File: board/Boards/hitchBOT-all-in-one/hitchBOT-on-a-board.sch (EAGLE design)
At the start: 25 parts, among them Q1 SPD30P06PTO252, Q2 SPD30P06PTO252

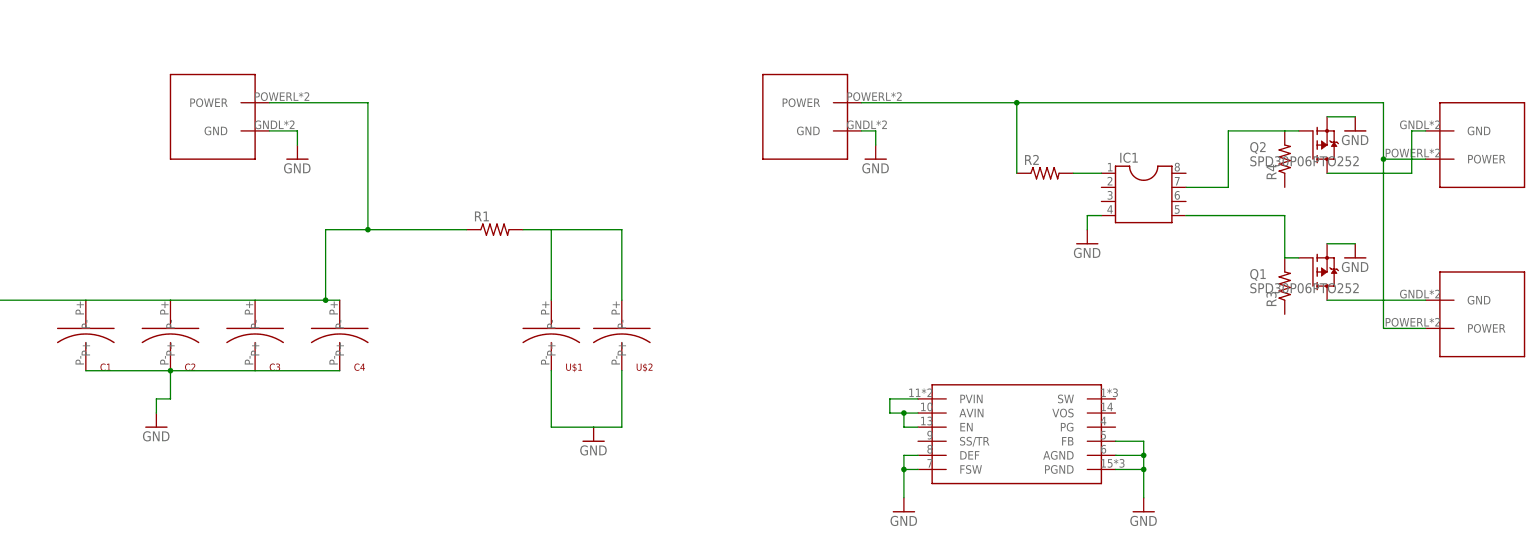
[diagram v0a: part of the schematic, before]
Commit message: finished initial rough copy of the board, need to add LEDs and writing
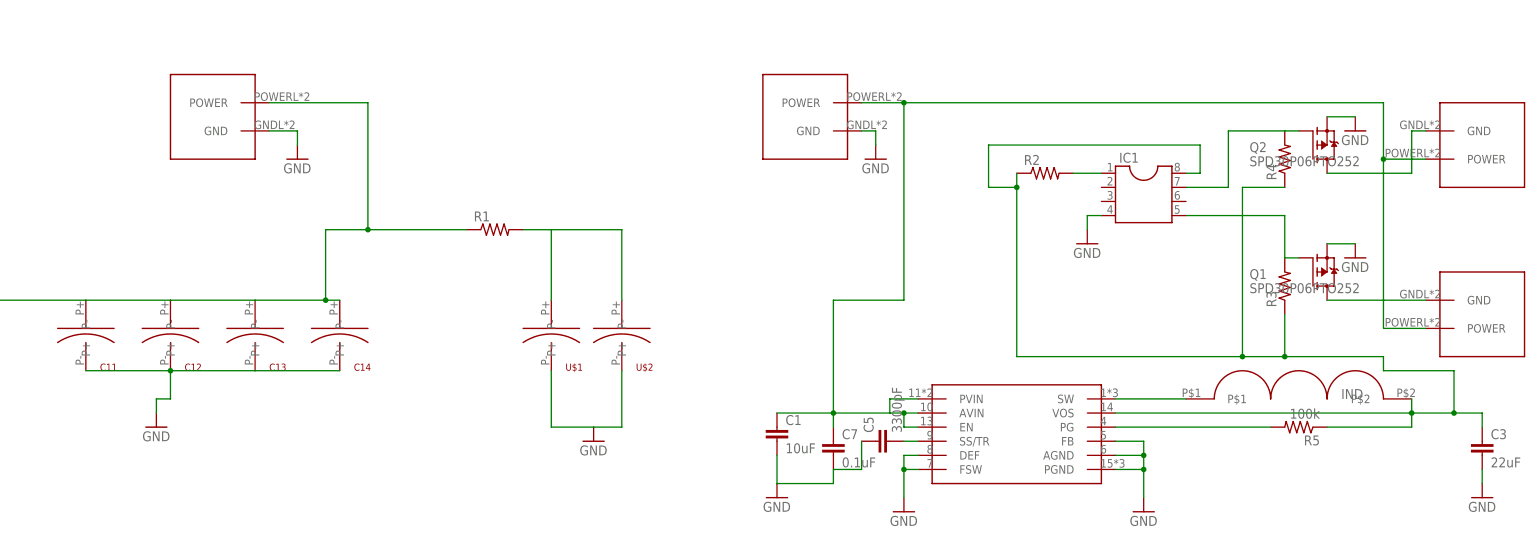
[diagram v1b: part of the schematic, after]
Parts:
- added C11, C13: SMD-CAP-NICHICON-8MM, macgrid:SMD-CAP-NICHICON-8MM
- added C5: 3300pF, rcl:C-EUC0603
- added C7: 0.1uF, rcl:C-EUC0603
- added R5: 100k, resistor:R-US_R1206
- added U$15: DR73-2R2-R, macgrid:DR73-2R2-R
- C1: value SMD-CAP-NICHICON-8MM -> 10uF; device macgrid:SMD-CAP-NICHICON-8MM -> eagle-ltspice:CC1210
- C3: value SMD-CAP-NICHICON-8MM -> 22uF; device macgrid:SMD-CAP-NICHICON-8MM -> rcl:C-EUC0805
- renumbered C2 to C12, C4 to C14
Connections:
- removed net N$12: U$14.AVIN, U$14.EN, U$14.PVIN
- new net N$14: U$14.SW, U$15.P$1
- new net N$15: C3.1, IC1.8, R2.1, R3.1, R4.1, R5.1, U$14.VOS, U$15.P$2
- new net N$16: R5.2, U$14.PG
- new net N$17: C5.2, U$14.SS/TR
- net GND: now also C1.2, C11.P-, C13.P-, C3.2, C5.1, C7.2; no longer C1.P-, C3.P-
- net N$1: now also C11.P+, C13.P+; no longer C1.P+, C3.P+
- net N$8: now also C1.1, C7.1, U$14.AVIN, U$14.EN, U$14.PVIN; no longer R2.1

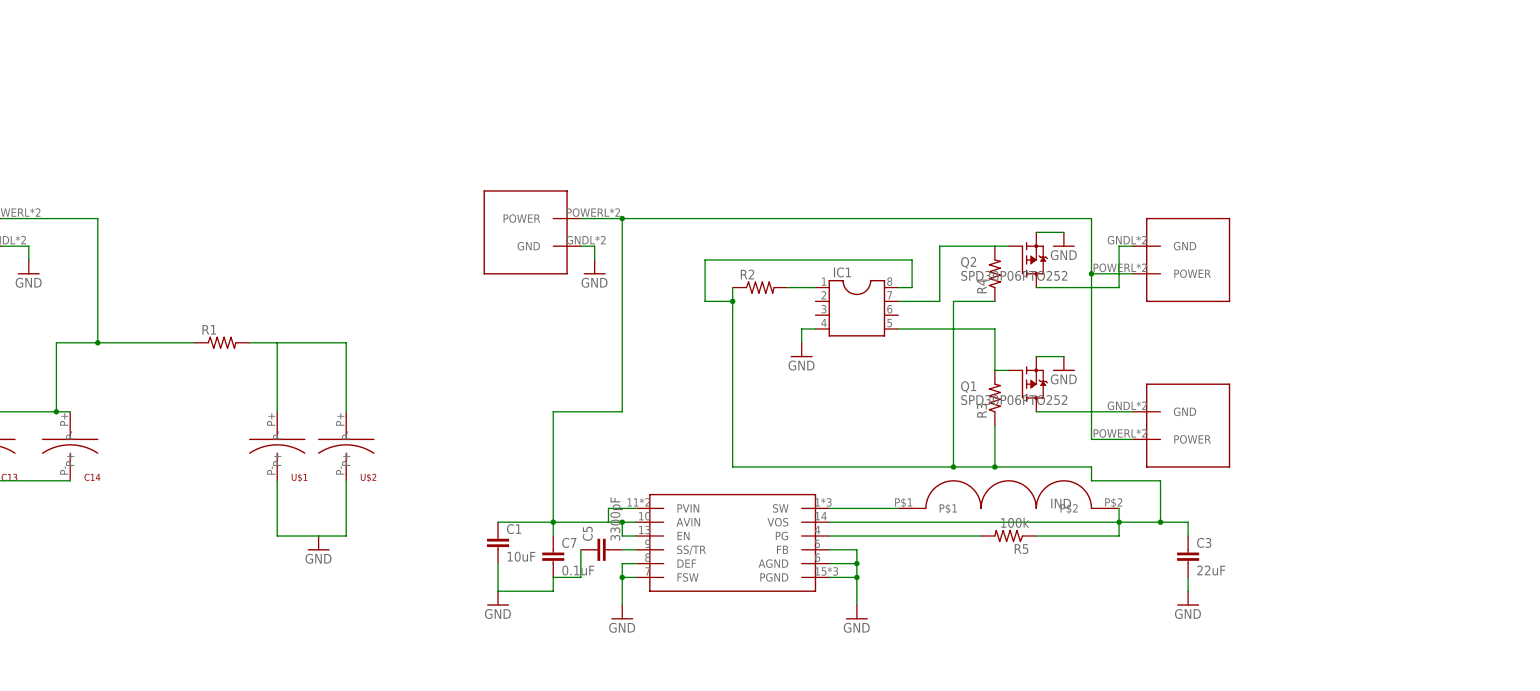
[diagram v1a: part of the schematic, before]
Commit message: added status LED and molex power adapters for all three voltage areas
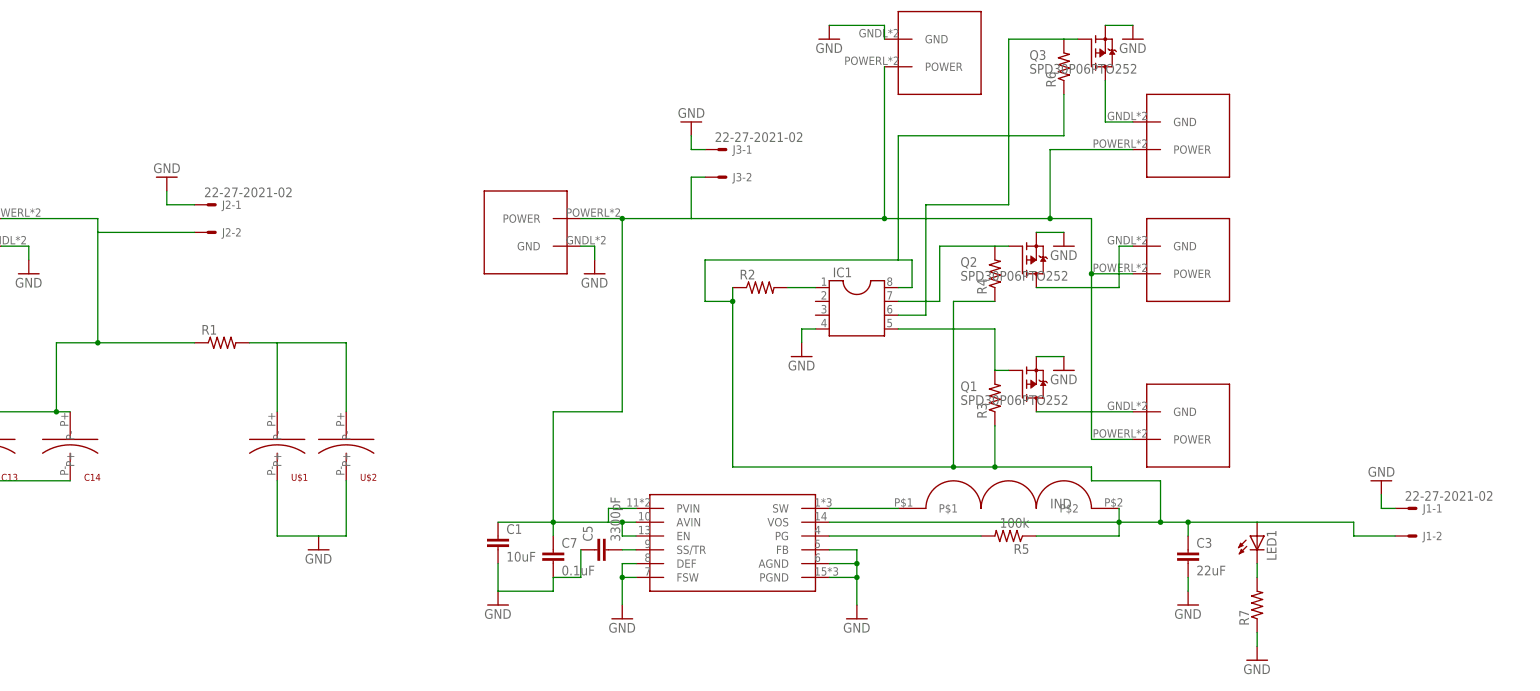
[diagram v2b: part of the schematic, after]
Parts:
- added J1, J2, J3: 22-27-2021-02, con-molex:22-27-2021-02
- added LED1: (no value), led:LEDCHIPLED_1206
- added Q3: SPD30P06PTO252, transistor-fet:SPD30P06PTO252
- added R6: (no value), resistor:R-US_R1206
- added R7: (no value), rcl:R-US_R1206
- added U$16, U$17: 2X2-MOLEX, Molex:2X2-MOLEX
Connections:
- new net N$18: Q3.D, U$17.GND
- new net N$19: IC1.6, Q3.G, R6.2
- new net N$20: LED1.C, R7.2
- net GND: now also J1-1.S, J2-1.S, J3-1.S, Q3.S, R7.1, U$16.GND
- net N$1: now also J2-2.S
- net N$15: now also J1-2.S, LED1.A, R6.1
- net N$8: now also J3-2.S, U$16.POWER, U$17.POWER
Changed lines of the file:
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@@
 <part name="C5" library="rcl" deviceset="C-EU" device="C0603" value="3300pF"/>
 <part name="C7" library="rcl" deviceset="C-EU" device="C0603" value="0.1uF"/>
+<part name="U$16" library="Molex" deviceset="2X2-MOLEX" device=""/>
+<part name="U$17" library="Molex" deviceset="2X2-MOLEX" device=""/>
+<part name="GND15" library="supply1" deviceset="GND" device=""/>
+<part name="Q3" library="transistor-fet" deviceset="SPD30P06P" device="TO252"/>
+<part name="R6" library="resistor" deviceset="R-US_" device="R1206"/>
+<part name="GND16" library="supply1" deviceset="GND" device=""/>
+<part name="LED1" library="led" deviceset="LED" device="CHIPLED_1206"/>
+<part name="R7" library="rcl" deviceset="R-US_" device="R1206"/>
+<part name="GND17" library="supply1" deviceset="GND" device=""/>
+<part name="J1" library="con-molex" deviceset="22-?-02" device="27-2021"/>
+<part name="J2" library="con-molex" deviceset="22-?-02" device="27-2021"/>
+<part name="J3" library="con-molex" deviceset="22-?-02" device="27-2021"/>
+<part name="GND18" library="supply1" deviceset="GND" device=""/>
+<part name="GND19" library="supply1" deviceset="GND" device=""/>
+<part name="GND20" library="supply1" deviceset="GND" device=""/>
 </parts>
 <sheets>
@@
 <instance part="C5" gate="G$1" x="190.5" y="38.1" rot="R90"/>
 <instance part="C7" gate="G$1" x="182.88" y="38.1"/>
+<instance part="U$16" gate="G$1" x="256.54" y="129.54" rot="R90"/>
+<instance part="U$17" gate="G$1" x="302.26" y="114.3" rot="R90"/>
+<instance part="GND15" gate="1" x="233.68" y="132.08"/>
+<instance part="Q3" gate="G$1" x="281.94" y="129.54"/>
+<instance part="R6" gate="G$1" x="276.86" y="127" rot="R90"/>
+<instance part="GND16" gate="1" x="289.56" y="132.08"/>
+<instance part="LED1" gate="G$1" x="312.42" y="40.64"/>
+<instance part="R7" gate="G$1" x="312.42" y="27.94" rot="R90"/>
+<instance part="GND17" gate="1" x="312.42" y="17.78"/>
+<instance part="J1" gate="-1" x="340.36" y="45.72"/>
+<instance part="J1" gate="-2" x="340.36" y="40.64"/>
+<instance part="J2" gate="-1" x="119.38" y="101.6"/>
+<instance part="J2" gate="-2" x="119.38" y="96.52"/>
+<instance part="J3" gate="-1" x="213.36" y="111.76"/>
+<instance part="J3" gate="-2" x="213.36" y="106.68"/>
+<instance part="GND18" gate="1" x="111.76" y="106.68" rot="R180"/>
+<instance part="GND19" gate="1" x="208.28" y="116.84" rot="R180"/>
+<instance part="GND20" gate="1" x="335.28" y="50.8" rot="R180"/>
 </instances>
 <busses>
@@
 <pinref part="U$10" gate="G$1" pin="POWER"/>
 <wire x1="81.28" y1="99.06" x2="99.06" y2="99.06" width="0.1524" layer="91"/>
-<wire x1="99.06" y1="99.06" x2="99.06" y2="76.2" width="0.1524" layer="91"/>
+<wire x1="99.06" y1="99.06" x2="99.06" y2="96.52" width="0.1524" layer="91"/>
 <junction x="99.06" y="76.2"/>
+<pinref part="J2" gate="-2" pin="S"/>
+<wire x1="99.06" y1="96.52" x2="99.06" y2="76.2" width="0.1524" layer="91"/>
+<wire x1="116.84" y1="96.52" x2="99.06" y2="96.52" width="0.1524" layer="91"/>
 </segment>
 </net>
@@
 <pinref part="GND14" gate="1" pin="GND"/>
 <wire x1="299.72" y1="33.02" x2="299.72" y2="30.48" width="0.1524" layer="91"/>
+</segment>
+<segment>
+<pinref part="U$16" gate="G$1" pin="GND"/>
+<pinref part="GND15" gate="1" pin="GND"/>
+<wire x1="243.84" y1="132.08" x2="243.84" y2="134.62" width="0.1524" layer="91"/>
+<wire x1="243.84" y1="134.62" x2="233.68" y2="134.62" width="0.1524" layer="91"/>
+</segment>
+<segment>
+<pinref part="Q3" gate="G$1" pin="S"/>
+<pinref part="GND16" gate="1" pin="GND"/>
+<wire x1="284.48" y1="134.62" x2="289.56" y2="134.62" width="0.1524" layer="91"/>
+</segment>
+<segment>
+<pinref part="R7" gate="G$1" pin="1"/>
+<pinref part="GND17" gate="1" pin="GND"/>
+<wire x1="312.42" y1="22.86" x2="312.42" y2="20.32" width="0.1524" layer="91"/>
+</segment>
+<segment>
+<pinref part="J2" gate="-1" pin="S"/>
+<pinref part="GND18" gate="1" pin="GND"/>
+<wire x1="116.84" y1="101.6" x2="111.76" y2="101.6" width="0.1524" layer="91"/>
+<wire x1="111.76" y1="101.6" x2="111.76" y2="104.14" width="0.1524" layer="91"/>
+</segment>
+<segment>
+<pinref part="J3" gate="-1" pin="S"/>
+<pinref part="GND19" gate="1" pin="GND"/>
+<wire x1="210.82" y1="111.76" x2="208.28" y2="111.76" width="0.1524" layer="91"/>
+<wire x1="208.28" y1="111.76" x2="208.28" y2="114.3" width="0.1524" layer="91"/>
+</segment>
+<segment>
+<pinref part="J1" gate="-1" pin="S"/>
+<pinref part="GND20" gate="1" pin="GND"/>
+<wire x1="337.82" y1="45.72" x2="335.28" y2="45.72" width="0.1524" layer="91"/>
+<wire x1="335.28" y1="45.72" x2="335.28" y2="48.26" width="0.1524" layer="91"/>
 </segment>
 </net>
@@
 <pinref part="U$11" gate="G$1" pin="POWER"/>
 <wire x1="187.96" y1="99.06" x2="195.58" y2="99.06" width="0.1524" layer="91"/>
-<wire x1="195.58" y1="99.06" x2="281.94" y2="99.06" width="0.1524" layer="91"/>
+<wire x1="195.58" y1="99.06" x2="208.28" y2="99.06" width="0.1524" layer="91"/>
+<wire x1="208.28" y1="99.06" x2="243.84" y2="99.06" width="0.1524" layer="91"/>
+<wire x1="243.84" y1="99.06" x2="274.32" y2="99.06" width="0.1524" layer="91"/>
+<wire x1="274.32" y1="99.06" x2="281.94" y2="99.06" width="0.1524" layer="91"/>
 <wire x1="281.94" y1="99.06" x2="281.94" y2="88.9" width="0.1524" layer="91"/>
 <pinref part="U$12" gate="G$1" pin="POWER"/>
@@
 <wire x1="182.88" y1="63.5" x2="182.88" y2="43.18" width="0.1524" layer="91"/>
 <junction x="195.58" y="99.06"/>
+<pinref part="U$16" gate="G$1" pin="POWER"/>
+<wire x1="243.84" y1="127" x2="243.84" y2="99.06" width="0.1524" layer="91"/>
+<pinref part="U$17" gate="G$1" pin="POWER"/>
+<wire x1="289.56" y1="111.76" x2="274.32" y2="111.76" width="0.1524" layer="91"/>
+<wire x1="274.32" y1="111.76" x2="274.32" y2="99.06" width="0.1524" layer="91"/>
+<junction x="274.32" y="99.06"/>
+<junction x="243.84" y="99.06"/>
+<pinref part="J3" gate="-2" pin="S"/>
+<wire x1="210.82" y1="106.68" x2="208.28" y2="106.68" width="0.1524" layer="91"/>
+<wire x1="208.28" y1="106.68" x2="208.28" y2="99.06" width="0.1524" layer="91"/>
 </segment>
 </net>
@@
 <wire x1="246.38" y1="86.36" x2="248.92" y2="86.36" width="0.1524" layer="91"/>
 <wire x1="248.92" y1="86.36" x2="248.92" y2="91.44" width="0.1524" layer="91"/>
-<wire x1="248.92" y1="91.44" x2="210.82" y2="91.44" width="0.1524" layer="91"/>
+<wire x1="248.92" y1="91.44" x2="246.38" y2="91.44" width="0.1524" layer="91"/>
+<wire x1="246.38" y1="91.44" x2="210.82" y2="91.44" width="0.1524" layer="91"/>
 <wire x1="210.82" y1="91.44" x2="210.82" y2="83.82" width="0.1524" layer="91"/>
 <wire x1="210.82" y1="83.82" x2="215.9" y2="83.82" width="0.1524" layer="91"/>
@@
 <junction x="264.16" y="53.34"/>
 <junction x="294.64" y="43.18"/>
+<pinref part="R6" gate="G$1" pin="1"/>
+<wire x1="276.86" y1="121.92" x2="276.86" y2="114.3" width="0.1524" layer="91"/>
+<wire x1="276.86" y1="114.3" x2="246.38" y2="114.3" width="0.1524" layer="91"/>
+<wire x1="246.38" y1="114.3" x2="246.38" y2="91.44" width="0.1524" layer="91"/>
+<pinref part="LED1" gate="G$1" pin="A"/>
+<wire x1="312.42" y1="43.18" x2="299.72" y2="43.18" width="0.1524" layer="91"/>
+<junction x="299.72" y="43.18"/>
+<wire x1="312.42" y1="43.18" x2="330.2" y2="43.18" width="0.1524" layer="91"/>
+<wire x1="330.2" y1="43.18" x2="330.2" y2="40.64" width="0.1524" layer="91"/>
+<pinref part="J1" gate="-2" pin="S"/>
+<wire x1="330.2" y1="40.64" x2="337.82" y2="40.64" width="0.1524" layer="91"/>
 </segment>
 </net>
@@
 </segment>
 </net>
+<net name="N$19" class="0">
+<segment>
+<pinref part="Q3" gate="G$1" pin="G"/>
+<pinref part="R6" gate="G$1" pin="2"/>
+<wire x1="279.4" y1="132.08" x2="276.86" y2="132.08" width="0.1524" layer="91"/>
+<wire x1="276.86" y1="132.08" x2="266.7" y2="132.08" width="0.1524" layer="91"/>
+<wire x1="266.7" y1="132.08" x2="266.7" y2="101.6" width="0.1524" layer="91"/>
+<wire x1="266.7" y1="101.6" x2="251.46" y2="101.6" width="0.1524" layer="91"/>
+<wire x1="251.46" y1="101.6" x2="251.46" y2="81.28" width="0.1524" layer="91"/>
+<pinref part="IC1" gate="G$1" pin="6"/>
+<wire x1="251.46" y1="81.28" x2="246.38" y2="81.28" width="0.1524" layer="91"/>
+</segment>
+</net>
+<net name="N$18" class="0">
+<segment>
+<pinref part="Q3" gate="G$1" pin="D"/>
+<pinref part="U$17" gate="G$1" pin="GND"/>
+<wire x1="284.48" y1="124.46" x2="284.48" y2="116.84" width="0.1524" layer="91"/>
+<wire x1="284.48" y1="116.84" x2="289.56" y2="116.84" width="0.1524" layer="91"/>
+</segment>
+</net>
+<net name="N$20" class="0">
+<segment>
+<pinref part="R7" gate="G$1" pin="2"/>
+<pinref part="LED1" gate="G$1" pin="C"/>
+<wire x1="312.42" y1="33.02" x2="312.42" y2="35.56" width="0.1524" layer="91"/>
+</segment>
+</net>
